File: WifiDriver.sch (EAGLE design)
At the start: 8 parts, among them U1 ESP32-DEVKITC-32U, U2 ESP32-DEVKITC-32U, U3 DS18B20

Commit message: Adding files
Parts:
- removed JP2, JP4, JP5: (no value), pinhead:PINHD-1X5
- added R2, R3, R4, R5: 0, adafruit:R-US_R0805
- added U$1: GPS_MOD, brandon_parts:GPS_MOD
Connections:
- new net ESP_A_RX: R3.1, U1.IO27
- new net ESP_A_TX: R2.1, U1.IO14
- new net ESP_B_RX: R4.2, U2.IO27
- new net ESP_B_TX: R5.2, U2.IO14
- new net N$2: R3.2, R5.1
- new net N$3: U1.IO32, U2.IO13
- net 5V: now also R1.2, U$1.VCC; no longer JP2.5, JP4.3, JP5.3
- net DQ: now also R1.1, U1.IO4, U3.DQ; no longer R1.2
- net ESP32_1_RX: no longer JP4.4
- net ESP32_1_TX: no longer JP4.5
- net ESP32_2_RX: no longer JP5.4
- net ESP32_2_TX: no longer JP5.5
- net GND: now also U$1.GND; no longer JP2.4, JP4.1, JP5.1
- net GPS_RX: now also U$1.RXD; no longer JP2.2
- net GPS_TX: now also U$1.TXD; no longer JP2.3
- net N$1: now also R2.2, R4.1; no longer R1.1, U3.DQ
- net PPS: now also U$1.PPS; no longer JP2.1
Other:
- moved on the sheet: U1, U2

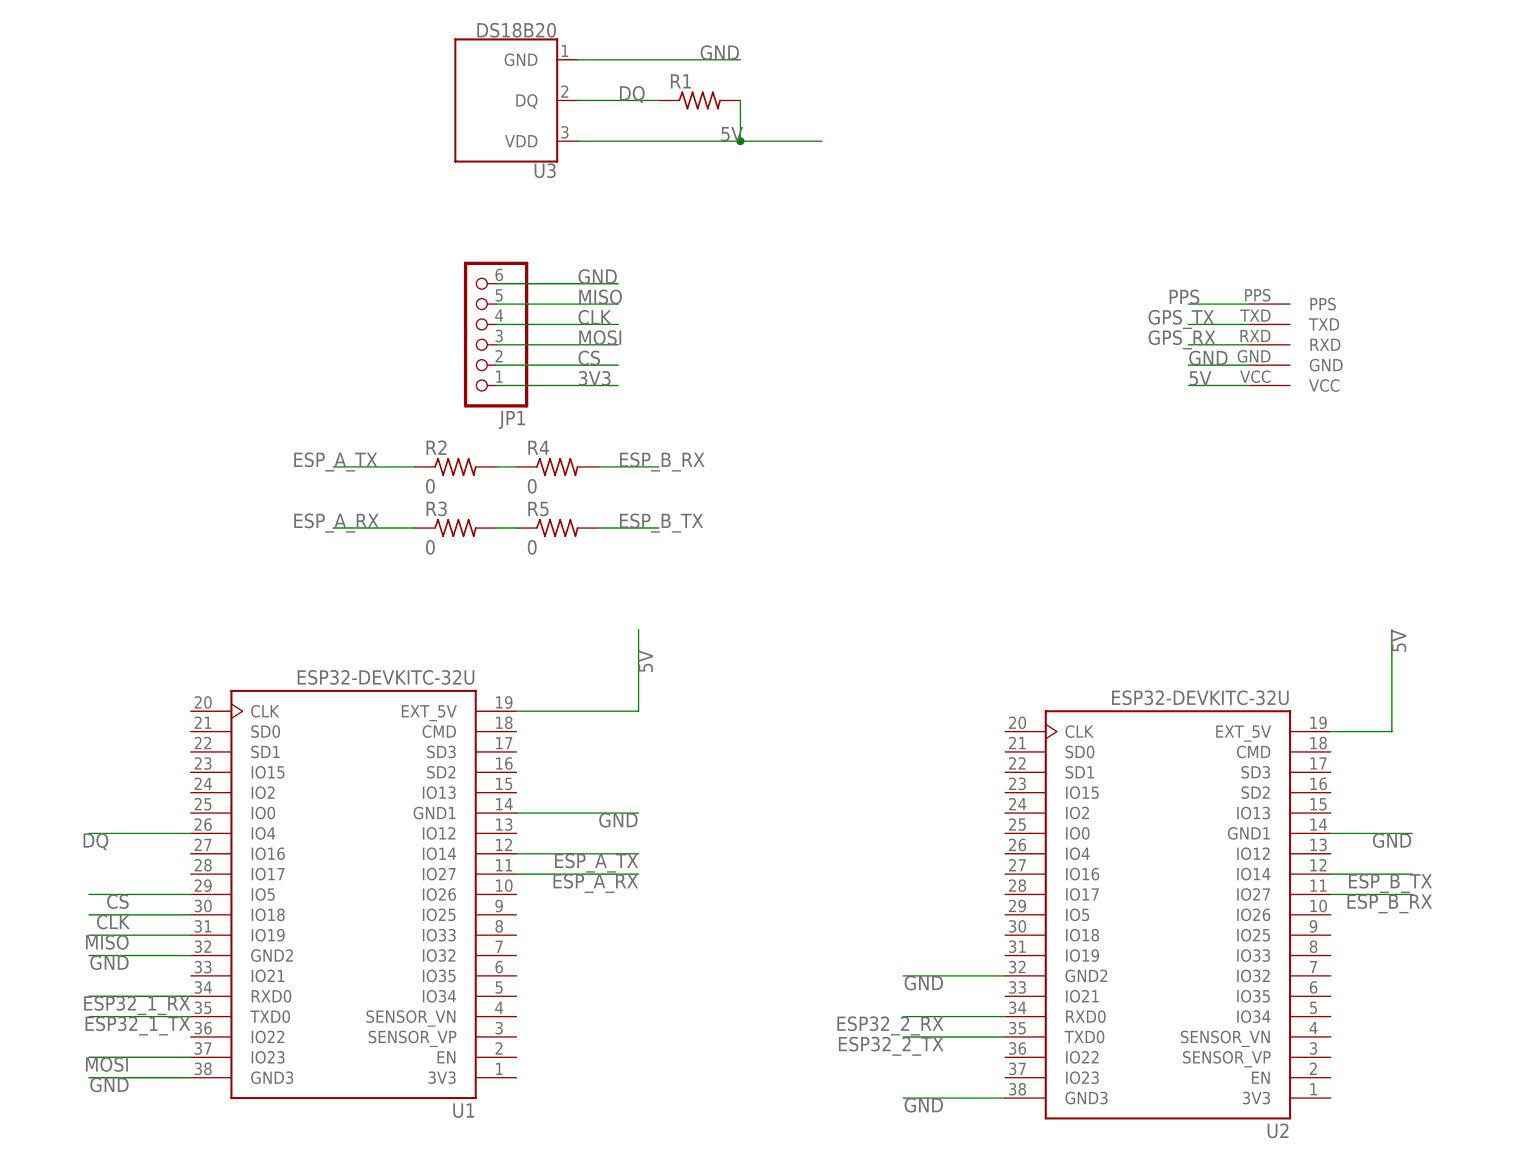
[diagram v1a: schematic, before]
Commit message: Updated with wardriver_v3 pinout from original author
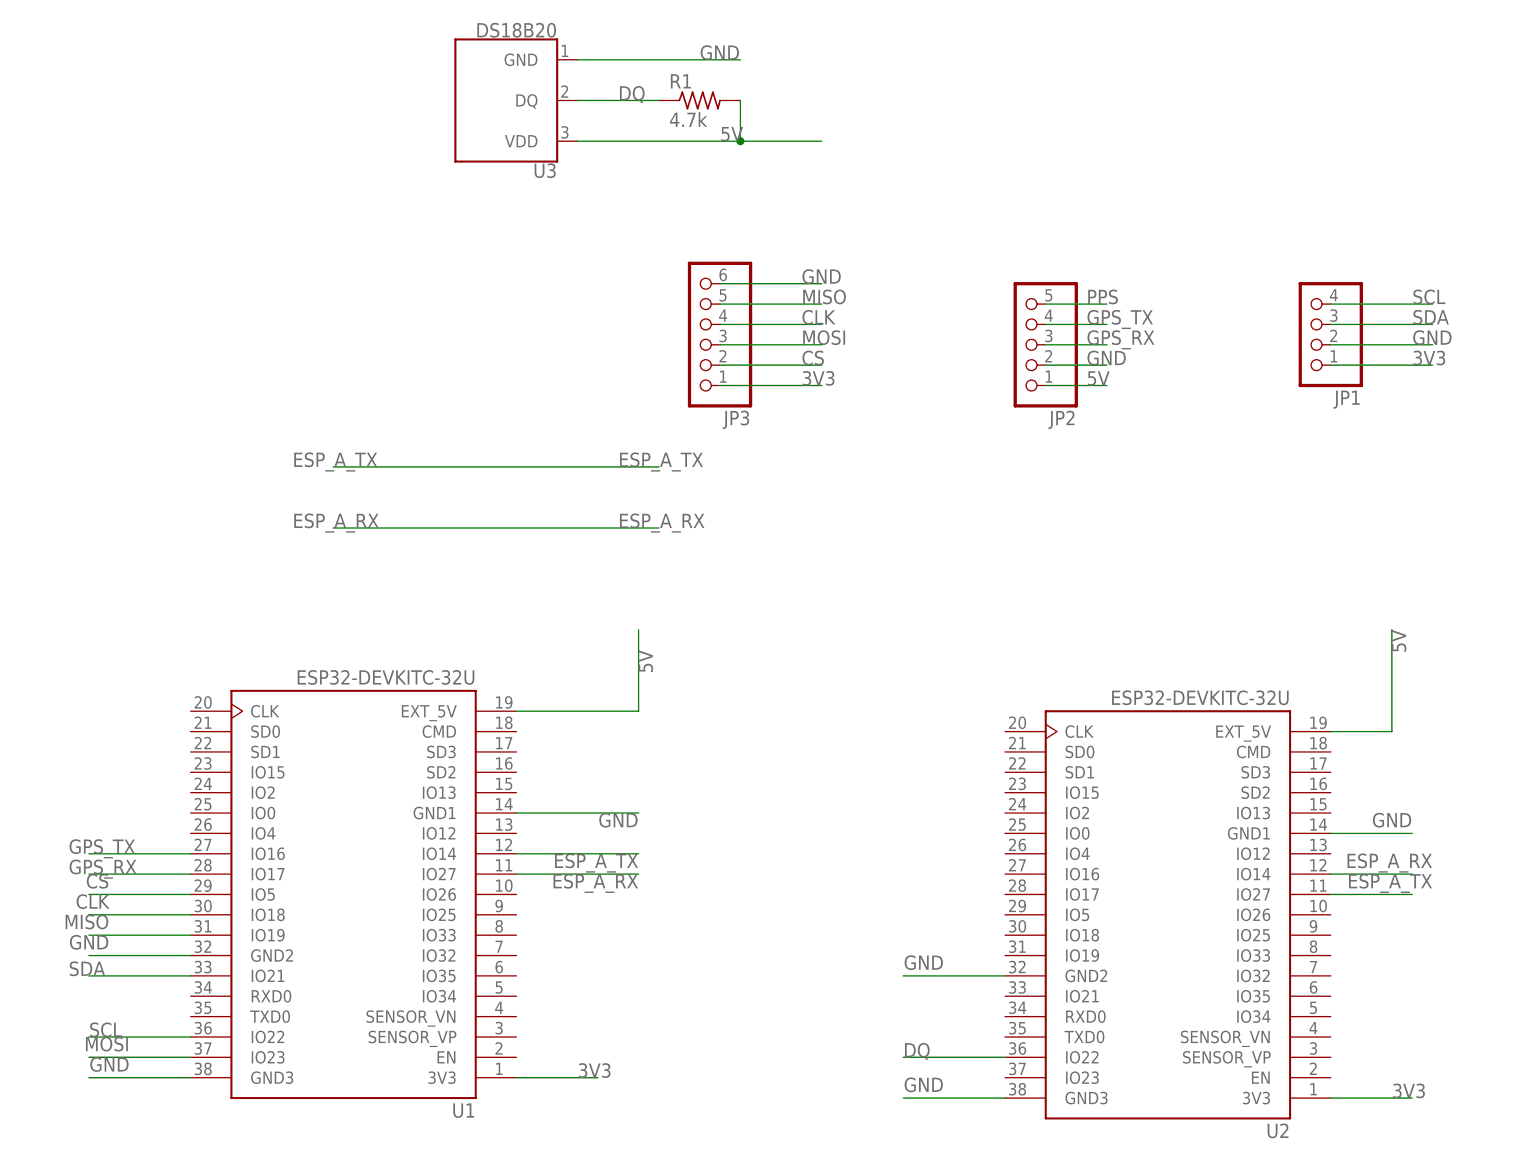
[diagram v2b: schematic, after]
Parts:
- removed R2, R3, R4, R5: 0, adafruit:R-US_R0805
- removed U$1: GPS_MOD, brandon_parts:GPS_MOD
- added JP2: (no value), pinhead:PINHD-1X5
- added JP3: (no value), pinhead:PINHD-1X6
- JP1: device adafruit:PINHD-1X6 -> pinhead:PINHD-1X4
- R1: value (none) -> 4.7k; device adafruit:R-US_M0805 -> adafruit:FLIPFLOP-RES
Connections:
- removed net ESP32_1_RX: U1.RXD0
- removed net ESP32_1_TX: U1.TXD0
- removed net ESP32_2_RX: U2.RXD0
- removed net ESP32_2_TX: U2.TXD0
- removed net ESP_B_RX: R4.2, U2.IO27
- removed net ESP_B_TX: R5.2, U2.IO14
- removed net N$1: R2.2, R4.1
- removed net N$2: R3.2, R5.1
- removed net N$3: U1.IO32, U2.IO13
- new net SCL: JP1.4, U1.IO22
- new net SDA: JP1.3, U1.IO21
- net 3V3: now also JP3.1, U1.3V3, U2.3V3
- net 5V: now also JP2.1; no longer U$1.VCC
- net CLK: now also JP3.4; no longer JP1.4
- net CS: now also JP3.2; no longer JP1.2
- net DQ: now also U2.IO22; no longer U1.IO4
- net ESP_A_RX: now also U2.IO14; no longer R3.1
- net ESP_A_TX: now also U2.IO27; no longer R2.1
- net GND: now also JP1.2, JP2.2, JP3.6; no longer JP1.6, U$1.GND
- net GPS_RX: now also JP2.3, U1.IO17; no longer U$1.RXD
- net GPS_TX: now also JP2.4, U1.IO16; no longer U$1.TXD
- net MISO: now also JP3.5; no longer JP1.5
- net MOSI: now also JP3.3; no longer JP1.3
- net PPS: now also JP2.5; no longer U$1.PPS
